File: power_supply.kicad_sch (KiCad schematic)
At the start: 9 parts

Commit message: fixes & doc
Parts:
- gave numbers to parts that had none: 7
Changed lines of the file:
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@@
 		(dnp no)
 		(fields_autoplaced yes)
-		(property "Reference" "#PWR?"
+		(property "Reference" "#PWR0185"
 			(at 62.23 124.46 0)
 			(effects
@@
 		(dnp no)
 		(fields_autoplaced yes)
-		(property "Reference" "U?"
+		(property "Reference" "U5"
 			(at 209.55 106.68 0)
 			(effects
@@
 		(dnp no)
 		(fields_autoplaced yes)
-		(property "Reference" "#PWR?"
+		(property "Reference" "#PWR0186"
 			(at 77.47 142.24 0)
 			(effects
@@
 		(dnp no)
 		(fields_autoplaced yes)
-		(property "Reference" "#PWR?"
+		(property "Reference" "#PWR0223"
 			(at 177.8 128.27 0)
 			(effects
@@
 		(dnp no)
 		(fields_autoplaced yes)
-		(property "Reference" "C?"
+		(property "Reference" "C184"
 			(at 137.16 107.9499 0)
 			(effects
@@
 		(dnp no)
 		(fields_autoplaced yes)
-		(property "Reference" "#PWR?"
+		(property "Reference" "#PWR0221"
 			(at 49.53 110.49 0)
 			(effects
@@
 		(dnp no)
 		(fields_autoplaced yes)
-		(property "Reference" "C?"
+		(property "Reference" "C182"
 			(at 71.12 153.6699 0)
 			(effects
@@
 		(dnp no)
 		(fields_autoplaced yes)
-		(property "Reference" "#PWR?"
+		(property "Reference" "#PWR0191"
 			(at 209.55 143.51 0)
 			(effects
@@
 		(dnp no)
 		(fields_autoplaced yes)
-		(property "Reference" "#PWR?"
+		(property "Reference" "#PWR0189"
 			(at 245.11 123.19 0)
 			(effects
@@
 		(dnp no)
 		(fields_autoplaced yes)
-		(property "Reference" "#PWR?"
+		(property "Reference" "#PWR0187"
 			(at 134.62 120.65 0)
 			(effects
@@
 		(dnp no)
 		(fields_autoplaced yes)
-		(property "Reference" "#PWR?"
+		(property "Reference" "#PWR0188"
 			(at 143.51 110.49 0)
 			(effects
@@
 		(dnp no)
 		(fields_autoplaced yes)
-		(property "Reference" "C?"
+		(property "Reference" "C187"
 			(at 247.65 125.7299 0)
 			(effects
@@
 		(dnp no)
 		(fields_autoplaced yes)
-		(property "Reference" "#PWR?"
+		(property "Reference" "#PWR0183"
 			(at 123.19 158.75 0)
 			(effects
@@
 		(dnp no)
 		(fields_autoplaced yes)
-		(property "Reference" "C?"
+		(property "Reference" "C183"
 			(at 64.77 110.4899 0)
 			(effects
@@
 		(dnp no)
 		(fields_autoplaced yes)
-		(property "Reference" "C?"
+		(property "Reference" "C186"
 			(at 180.34 128.2699 0)
 			(effects
@@
 		(dnp no)
 		(fields_autoplaced yes)
-		(property "Reference" "U?"
+		(property "Reference" "U4"
 			(at 102.87 96.52 0)
 			(effects
@@
 		(dnp no)
 		(fields_autoplaced yes)
-		(property "Reference" "R6"
+		(property "Reference" "R?"
 			(at 266.7 126.9999 0)
 			(effects
@@
 				(path "/092c92d2-76d4-44c2-8c00-1353e9f14223"
 					(reference "R6")
+					(unit 1)
+				)
+			)
+			(project "75he"
+				(path "/0edb4e17-93a4-4f7b-ad91-3a5c72b69d23/f26c38a6-65b7-4d4b-b531-bf41915dd707"
+					(reference "R?")
 					(unit 1)
 				)
@@
 		(on_board yes)
 		(dnp no)
-		(property "Reference" "D1"
+		(property "Reference" "D?"
 			(at 255.27 116.586 90)
 			(effects
@@
 				(path "/092c92d2-76d4-44c2-8c00-1353e9f14223"
 					(reference "D1")
+					(unit 1)
+				)
+			)
+			(project "75he"
+				(path "/0edb4e17-93a4-4f7b-ad91-3a5c72b69d23/f26c38a6-65b7-4d4b-b531-bf41915dd707"
+					(reference "D?")
 					(unit 1)
 				)
@@
 		(dnp no)
 		(fields_autoplaced yes)
-		(property "Reference" "#PWR?"
+		(property "Reference" "#PWR0182"
 			(at 68.58 168.91 0)
 			(effects

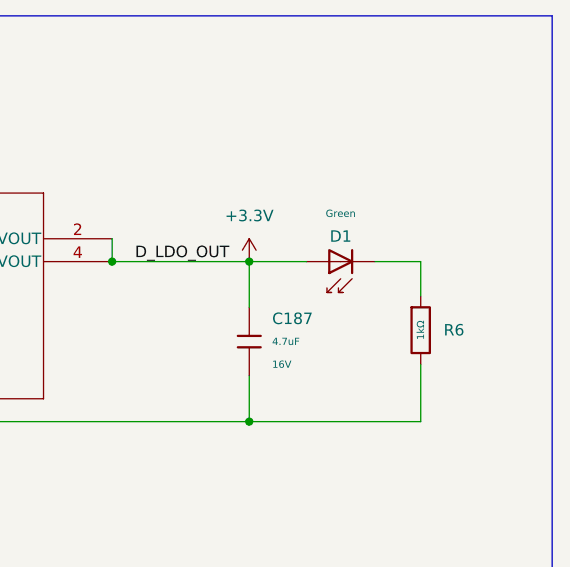
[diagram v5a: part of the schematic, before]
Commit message: Add WS2812 footprints, resistors and net names
Replace generic switch footprints with proper SMD components and metadata: add WS2812B RGB LED footprints (with pads, nets, 3D models and part/Datasheet/LCSC info), add many resistor footprints and detailed properties, and update net names for LED data lines (e.g. Net-(D201-DIN/DOUT) etc.). Also adjust footprint positions, pad assignments, sheet references (LED/HE Sensors), and footprint drawing/printer layers to match correct component geometry for assembly and BOM generation.
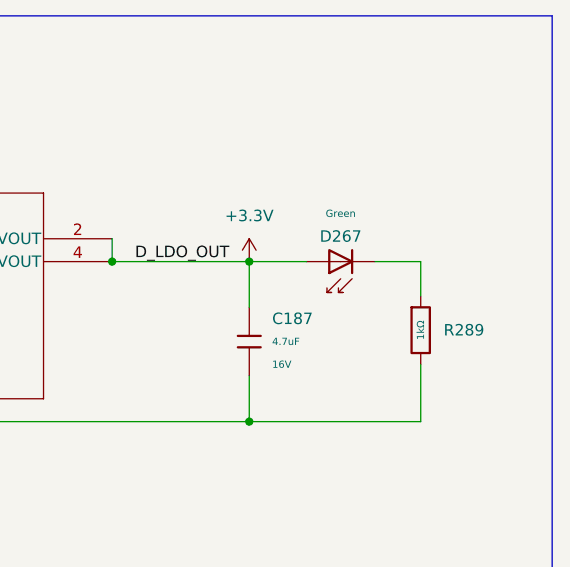
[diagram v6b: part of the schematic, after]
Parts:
- renumbered D1 to D267, R6 to R289
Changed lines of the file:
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@@
 		(dnp no)
 		(fields_autoplaced yes)
-		(property "Reference" "R?"
+		(property "Reference" "R289"
 			(at 266.7 126.9999 0)
 			(effects
@@
 			(project "75he"
 				(path "/0edb4e17-93a4-4f7b-ad91-3a5c72b69d23/f26c38a6-65b7-4d4b-b531-bf41915dd707"
-					(reference "R?")
+					(reference "R289")
 					(unit 1)
 				)
@@
 		(on_board yes)
 		(dnp no)
-		(property "Reference" "D?"
+		(property "Reference" "D267"
 			(at 255.27 116.586 90)
 			(effects
@@
 			(project "75he"
 				(path "/0edb4e17-93a4-4f7b-ad91-3a5c72b69d23/f26c38a6-65b7-4d4b-b531-bf41915dd707"
-					(reference "D?")
+					(reference "D267")
 					(unit 1)
 				)

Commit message: Update 0402 resistors to 680Ω and add libs
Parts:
- U4: footprint RGW0020A-IPC_A -> TPS7A4701RGWR:RGW0020A-IPC_A
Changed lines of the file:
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@@
 			(project "power_supply"
 				(path "/092c92d2-76d4-44c2-8c00-1353e9f14223"
-					(reference "#PWR?")
+					(reference "#PWR02")
 					(unit 1)
 				)
@@
 			(project "power_supply"
 				(path "/092c92d2-76d4-44c2-8c00-1353e9f14223"
-					(reference "U?")
+					(reference "U2")
 					(unit 1)
 				)
@@
 			(project "power_supply"
 				(path "/092c92d2-76d4-44c2-8c00-1353e9f14223"
-					(reference "#PWR?")
+					(reference "#PWR04")
 					(unit 1)
 				)
@@
 			(project "power_supply"
 				(path "/092c92d2-76d4-44c2-8c00-1353e9f14223"
-					(reference "#PWR?")
+					(reference "#PWR08")
 					(unit 1)
 				)
@@
 			(project "power_supply"
 				(path "/092c92d2-76d4-44c2-8c00-1353e9f14223"
-					(reference "C?")
+					(reference "C3")
 					(unit 1)
 				)
@@
 			(project "power_supply"
 				(path "/092c92d2-76d4-44c2-8c00-1353e9f14223"
-					(reference "#PWR?")
+					(reference "#PWR01")
 					(unit 1)
 				)
@@
 			(project "power_supply"
 				(path "/092c92d2-76d4-44c2-8c00-1353e9f14223"
-					(reference "C?")
+					(reference "C2")
 					(unit 1)
 				)
@@
 			(project "power_supply"
 				(path "/092c92d2-76d4-44c2-8c00-1353e9f14223"
-					(reference "#PWR?")
+					(reference "#PWR09")
 					(unit 1)
 				)
@@
 			(project "power_supply"
 				(path "/092c92d2-76d4-44c2-8c00-1353e9f14223"
-					(reference "#PWR?")
+					(reference "#PWR010")
 					(unit 1)
 				)
@@
 			(project "power_supply"
 				(path "/092c92d2-76d4-44c2-8c00-1353e9f14223"
-					(reference "#PWR?")
+					(reference "#PWR06")
 					(unit 1)
 				)
@@
 			(project "power_supply"
 				(path "/092c92d2-76d4-44c2-8c00-1353e9f14223"
-					(reference "#PWR?")
+					(reference "#PWR07")
 					(unit 1)
 				)
@@
 			(project "power_supply"
 				(path "/092c92d2-76d4-44c2-8c00-1353e9f14223"
-					(reference "C?")
+					(reference "C5")
 					(unit 1)
 				)
@@
 			(project "power_supply"
 				(path "/092c92d2-76d4-44c2-8c00-1353e9f14223"
-					(reference "#PWR?")
+					(reference "#PWR05")
 					(unit 1)
 				)
@@
 			(project "power_supply"
 				(path "/092c92d2-76d4-44c2-8c00-1353e9f14223"
-					(reference "C?")
+					(reference "C1")
 					(unit 1)
 				)
@@
 			(project "power_supply"
 				(path "/092c92d2-76d4-44c2-8c00-1353e9f14223"
-					(reference "C?")
+					(reference "C4")
 					(unit 1)
 				)
@@
 			)
 		)
-		(property "Footprint" "RGW0020A-IPC_A"
+		(property "Footprint" "TPS7A4701RGWR:RGW0020A-IPC_A"
 			(at 82.55 106.68 0)
 			(effects
@@
 			(project "power_supply"
 				(path "/092c92d2-76d4-44c2-8c00-1353e9f14223"
-					(reference "U?")
+					(reference "U1")
 					(unit 1)
 				)
@@
 			(project "power_supply"
 				(path "/092c92d2-76d4-44c2-8c00-1353e9f14223"
-					(reference "#PWR?")
-					(unit 1)
-				)
+					(reference "#PWR03")
+					(unit 1)
+				)

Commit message: clean schematics
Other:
- note removed: "Alimentation: Alimentation 3.3V: Alimentation (4V) TPS62913 (1.53$) 2 x 10uF (0.011$) 2.2nF (0.0011$) 470uF (0.0072$) 5 x 22uF (0.024$) FB (0.077$) R1 (0.037$) R2 (0.0012$) TOTAL = 1.8$ Analogique: TPS7A4701RGWR (1.71$) Numérique: LDL1117S33R (0.12$)"
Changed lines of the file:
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@@
-		)
-	)
-	(text "Alimentation:\n\nAlimentation 3.3V:\n\nAlimentation (4V)\n\nTPS62913 (1.53$)\n2 x 10uF (0.011$)\n2.2nF (0.0011$)\n470uF (0.0072$)\n5 x 22uF (0.024$)\nFB (0.077$)\nR1 (0.037$)\nR2 (0.0012$)\n\nTOTAL = 1.8$\n\n\nAnalogique:\n\nTPS7A4701RGWR (1.71$)\n\nNumérique:\n\nLDL1117S33R (0.12$)"
-		(exclude_from_sim no)
-		(at 239.014 51.308 0)
-		(effects
-			(font
-				(size 1.27 1.27)
-			)
-			(justify left)
 		)
 	)
